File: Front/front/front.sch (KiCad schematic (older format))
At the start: 12 parts, among them J1 JST PH 1mm 4-Pin Connector, J2 Conn_01x10_Male, SW1 SW_Push, U1 L293D

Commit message: Version 0.1.2 - First draft of front PCB complete
Signed-off-by: ray33ee <30669752+ray33ee@users.noreply.github.com>
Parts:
- added C2: 100nF, Capacitor_SMD:C_1206_3216Metric_Pad1.33x1.80mm_HandSolder, symbol Device:C
- J1: value JST PH 1mm 4-Pin Connector -> JST 1mm Connector
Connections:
- net labels added: Enable_Controlled, Enable_High, JST_PIN_1, JST_PIN_2, JST_PIN_3, JST_PIN_4, Motor_Supply_Pre
- wire segments 57 -> 60
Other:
- moved on the sheet: C1, D1, D2, R1, R2, R3, R4
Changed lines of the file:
@@
 P 6400 3850
 F 0 "J1" H 6372 3732 50  0000 R CNN
-F 1 "JST PH 1mm 4-Pin Connector" H 6372 3823 50  0000 R CNN
+F 1 "JST 1mm Connector" H 6372 3823 50  0000 R CNN
 F 2 "Connector_JST:JST_SH_SM04B-SRSS-TB_1x04-1MP_P1.00mm_Horizontal" H 6400 3850 50  0001 C CNN
 F 3 "~" H 6400 3850 50  0001 C CNN
@@
 	-1   0    0    1
 $EndComp
-Wire Wire Line
-	5650 3650 6200 3650
 $Comp
 L Device:R R1
 U 1 1 616B895B
-P 5250 2800
-F 0 "R1" H 5320 2846 50  0000 L CNN
-F 1 "1" H 5320 2755 50  0000 L CNN
-F 2 "Resistor_THT:R_Axial_DIN0204_L3.6mm_D1.6mm_P5.08mm_Horizontal" V 5180 2800 50  0001 C CNN
-F 3 "~" H 5250 2800 50  0001 C CNN
-	1    5250 2800
+P 5250 2200
+F 0 "R1" H 5320 2246 50  0000 L CNN
+F 1 "1" H 5320 2155 50  0000 L CNN
+F 2 "Resistor_THT:R_Axial_DIN0204_L3.6mm_D1.6mm_P5.08mm_Horizontal" V 5180 2200 50  0001 C CNN
+F 3 "~" H 5250 2200 50  0001 C CNN
+	1    5250 2200
 	1    0    0    -1
 $EndComp
@@
 L Device:R R3
 U 1 1 616B9582
-P 6300 2550
-F 0 "R3" V 6093 2550 50  0000 C CNN
-F 1 "270" V 6184 2550 50  0000 C CNN
-F 2 "Resistor_SMD:R_1206_3216Metric_Pad1.30x1.75mm_HandSolder" V 6230 2550 50  0001 C CNN
-F 3 "~" H 6300 2550 50  0001 C CNN
-	1    6300 2550
+P 6300 1950
+F 0 "R3" V 6093 1950 50  0000 C CNN
+F 1 "270" V 6184 1950 50  0000 C CNN
+F 2 "Resistor_SMD:R_1206_3216Metric_Pad1.30x1.75mm_HandSolder" V 6230 1950 50  0001 C CNN
+F 3 "~" H 6300 1950 50  0001 C CNN
+	1    6300 1950
 	0    1    1    0
 $EndComp
@@
 L Device:R R4
 U 1 1 616B98B9
-P 4200 3000
-F 0 "R4" H 4270 3046 50  0000 L CNN
-F 1 "10k" H 4270 2955 50  0000 L CNN
-F 2 "Resistor_SMD:R_1206_3216Metric_Pad1.30x1.75mm_HandSolder" V 4130 3000 50  0001 C CNN
-F 3 "~" H 4200 3000 50  0001 C CNN
-	1    4200 3000
-	1    0    0    -1
-$EndComp
-Wire Wire Line
-	5250 2950 5250 3050
+P 3800 2400
+F 0 "R4" H 3870 2446 50  0000 L CNN
+F 1 "10k" H 3870 2355 50  0000 L CNN
+F 2 "Resistor_SMD:R_1206_3216Metric_Pad1.30x1.75mm_HandSolder" V 3730 2400 50  0001 C CNN
+F 3 "~" H 3800 2400 50  0001 C CNN
+	1    3800 2400
+	1    0    0    -1
+$EndComp
+Wire Wire Line
+	5250 2350 5250 2450
 $Comp
 L Device:D_Zener D2
 U 1 1 616BE794
-P 5700 2550
-F 0 "D2" H 5700 2767 50  0000 C CNN
-F 1 "3.9v" H 5700 2676 50  0000 C CNN
-F 2 "Diode_SMD:D_T-1_P5.08mm_Horizontal_SurfaceMount" H 5700 2550 50  0001 C CNN
-F 3 "~" H 5700 2550 50  0001 C CNN
-	1    5700 2550
+P 5700 1950
+F 0 "D2" H 5700 2167 50  0000 C CNN
+F 1 "3.9v" H 5700 2076 50  0000 C CNN
+F 2 "Diode_SMD:D_T-1_P5.08mm_Horizontal_SurfaceMount" H 5700 1950 50  0001 C CNN
+F 3 "~" H 5700 1950 50  0001 C CNN
+	1    5700 1950
 	1    0    0    -1
 $EndComp
@@
 L Device:D_Zener D1
 U 1 1 616C048F
-P 5700 3050
-F 0 "D1" H 5700 3267 50  0000 C CNN
-F 1 "3.9v" H 5700 3176 50  0000 C CNN
-F 2 "Diode_SMD:D_T-1_P5.08mm_Horizontal_SurfaceMount" H 5700 3050 50  0001 C CNN
-F 3 "~" H 5700 3050 50  0001 C CNN
-	1    5700 3050
-	1    0    0    -1
-$EndComp
-Wire Wire Line
-	5550 2550 5250 2550
-Connection ~ 5250 2550
-Wire Wire Line
-	5250 2550 5250 2650
-Wire Wire Line
-	5250 3050 5550 3050
-Connection ~ 5250 3050
-Wire Wire Line
-	5250 3050 5250 3250
-Wire Wire Line
-	5850 2550 6000 2550
-Wire Wire Line
-	6150 3050 6000 3050
-Wire Wire Line
-	6450 3050 6450 2550
-Wire Wire Line
-	5050 3250 5050 2800
-Connection ~ 5050 2550
-Wire Wire Line
-	5050 2550 5250 2550
+P 5700 2450
+F 0 "D1" H 5700 2667 50  0000 C CNN
+F 1 "3.9v" H 5700 2576 50  0000 C CNN
+F 2 "Diode_SMD:D_T-1_P5.08mm_Horizontal_SurfaceMount" H 5700 2450 50  0001 C CNN
+F 3 "~" H 5700 2450 50  0001 C CNN
+	1    5700 2450
+	1    0    0    -1
+$EndComp
+Wire Wire Line
+	5550 1950 5250 1950
+Connection ~ 5250 1950
+Wire Wire Line
+	5250 1950 5250 2050
+Wire Wire Line
+	5250 2450 5550 2450
+Connection ~ 5250 2450
+Wire Wire Line
+	5850 1950 6000 1950
+Wire Wire Line
+	6150 2450 6000 2450
+Wire Wire Line
+	6450 2450 6450 1950
+Connection ~ 5050 1950
+Wire Wire Line
+	5050 1950 5250 1950
 $Comp
 L Device:R R2
 U 1 1 616B8410
-P 6300 3050
-F 0 "R2" V 6507 3050 50  0000 C CNN
-F 1 "270" V 6416 3050 50  0000 C CNN
-F 2 "Resistor_SMD:R_1206_3216Metric_Pad1.30x1.75mm_HandSolder" V 6230 3050 50  0001 C CNN
-F 3 "~" H 6300 3050 50  0001 C CNN
-	1    6300 3050
+P 6300 2450
+F 0 "R2" V 6507 2450 50  0000 C CNN
+F 1 "270" V 6416 2450 50  0000 C CNN
+F 2 "Resistor_SMD:R_1206_3216Metric_Pad1.30x1.75mm_HandSolder" V 6230 2450 50  0001 C CNN
+F 3 "~" H 6300 2450 50  0001 C CNN
+	1    6300 2450
 	0    -1   -1   0
 $EndComp
@@
 L power:GND #PWR0103
 U 1 1 616C51FA
-P 6800 3100
-F 0 "#PWR0103" H 6800 2850 50  0001 C CNN
-F 1 "GND" H 6805 2927 50  0000 C CNN
-F 2 "" H 6800 3100 50  0001 C CNN
-F 3 "" H 6800 3100 50  0001 C CNN
-	1    6800 3100
-	1    0    0    -1
-$EndComp
-Wire Wire Line
-	6800 3050 6800 3100
-Wire Wire Line
-	6000 2550 6000 2750
-Wire Wire Line
-	6000 2750 6350 2750
-Connection ~ 6000 2550
-Wire Wire Line
-	6000 2550 6150 2550
-Wire Wire Line
-	6000 3050 6000 3250
-Wire Wire Line
-	6000 3250 6350 3250
-Wire Wire Line
-	6450 3050 6800 3050
-Connection ~ 6450 3050
-Connection ~ 6000 3050
-Wire Wire Line
-	6000 3050 5850 3050
-Wire Wire Line
-	4200 2850 4200 2550
+P 6800 2500
+F 0 "#PWR0103" H 6800 2250 50  0001 C CNN
+F 1 "GND" H 6805 2327 50  0000 C CNN
+F 2 "" H 6800 2500 50  0001 C CNN
+F 3 "" H 6800 2500 50  0001 C CNN
+	1    6800 2500
+	1    0    0    -1
+$EndComp
+Wire Wire Line
+	6800 2450 6800 2500
+Wire Wire Line
+	6000 1950 6000 2150
+Wire Wire Line
+	6000 2150 6350 2150
+Connection ~ 6000 1950
+Wire Wire Line
+	6000 1950 6150 1950
+Wire Wire Line
+	6000 2450 6000 2650
+Wire Wire Line
+	6000 2650 6350 2650
+Wire Wire Line
+	6450 2450 6800 2450
+Connection ~ 6450 2450
+Connection ~ 6000 2450
+Wire Wire Line
+	6000 2450 5850 2450
+Wire Wire Line
+	3800 2250 3800 1950
 Wire Wire Line
 	4650 3650 4300 3650
@@
 	6500 4850 7050 4850
 Wire Wire Line
-	4200 2550 5050 2550
+	4200 1950 5050 1950
 $Comp
 L Connector:Conn_01x10_Male J2
@@
 Text Label 4350 4450 0    50   ~ 0
 Coil_B2
-Text Label 3350 3000 0    50   ~ 0
-Enable
-Text Label 6050 2750 0    50   ~ 0
+Text Label 4200 3250 1    50   ~ 0
+Enable_Controlled
+Text Label 6050 2150 0    50   ~ 0
 Diff_P1
-Text Label 6050 3250 0    50   ~ 0
+Text Label 6050 2650 0    50   ~ 0
 Diff_P2
 Text Label 8050 4100 0    50   ~ 0
@@
 	8000 4200 8550 4200
 Text Label 8050 4000 0    50   ~ 0
-Enable
+Enable_Controlled
 Text Label 8050 3800 0    50   ~ 0
 Diff_P2
@@
 	4000 4050 4000 4650
 Wire Wire Line
-	4200 3150 4200 3500
-Wire Wire Line
-	3800 3500 3800 3000
-Wire Wire Line
-	3200 3000 3800 3000
-Wire Wire Line
 	4950 5050 5050 5050
 Connection ~ 5050 5050
@@
 $EndComp
 Wire Wire Line
-	5650 3850 6200 3850
-Wire Wire Line
 	5650 4250 5700 4250
 Wire Wire Line
@@
 L Device:C C1
 U 1 1 61713F7C
-P 4550 2950
-F 0 "C1" H 4665 2996 50  0000 L CNN
-F 1 "100nF" H 4665 2905 50  0000 L CNN
-F 2 "Capacitor_SMD:C_1206_3216Metric_Pad1.33x1.80mm_HandSolder" H 4588 2800 50  0001 C CNN
-F 3 "~" H 4550 2950 50  0001 C CNN
-	1    4550 2950
-	1    0    0    -1
-$EndComp
-Connection ~ 5050 2800
-Wire Wire Line
-	5050 2800 5050 2550
+P 4650 2850
+F 0 "C1" H 4765 2896 50  0000 L CNN
+F 1 "100nF" H 4765 2805 50  0000 L CNN
+F 2 "Capacitor_SMD:C_1206_3216Metric_Pad1.33x1.80mm_HandSolder" H 4688 2700 50  0001 C CNN
+F 3 "~" H 4650 2850 50  0001 C CNN
+	1    4650 2850
+	1    0    0    -1
+$EndComp
+Connection ~ 5050 2200
+Wire Wire Line
+	5050 2200 5050 1950
 $Comp
 L power:GND #PWR0107
 U 1 1 61715C98
-P 4550 3100
-F 0 "#PWR0107" H 4550 2850 50  0001 C CNN
-F 1 "GND" H 4555 2927 50  0000 C CNN
-F 2 "" H 4550 3100 50  0001 C CNN
-F 3 "" H 4550 3100 50  0001 C CNN
-	1    4550 3100
-	1    0    0    -1
-$EndComp
-Wire Wire Line
-	4550 2800 5050 2800
+P 4650 3000
+F 0 "#PWR0107" H 4650 2750 50  0001 C CNN
+F 1 "GND" H 4655 2827 50  0000 C CNN
+F 2 "" H 4650 3000 50  0001 C CNN
+F 3 "" H 4650 3000 50  0001 C CNN
+	1    4650 3000
+	1    0    0    -1
+$EndComp
 $Comp
 L power:+5V #PWR0102
 U 1 1 616B66D4
-P 4200 2550
-F 0 "#PWR0102" H 4200 2400 50  0001 C CNN
-F 1 "+5V" H 4215 2723 50  0000 C CNN
-F 2 "" H 4200 2550 50  0001 C CNN
-F 3 "" H 4200 2550 50  0001 C CNN
-	1    4200 2550
-	1    0    0    -1
-$EndComp
-Connection ~ 4200 2550
+P 4200 1950
+F 0 "#PWR0102" H 4200 1800 50  0001 C CNN
+F 1 "+5V" H 4215 2123 50  0000 C CNN
+F 2 "" H 4200 1950 50  0001 C CNN
+F 3 "" H 4200 1950 50  0001 C CNN
+	1    4200 1950
+	1    0    0    -1
+$EndComp
+Text Label 5250 2600 0    50   ~ 0
+Motor_Supply_Pre
+Text Label 5750 3750 0    50   ~ 0
+JST_PIN_3
+Text Label 5750 3950 0    50   ~ 0
+JST_PIN_1
+Text Label 4350 4050 0    50   ~ 0
+Enable
+Text Label 3800 2850 2    50   ~ 0
+Enable_High
+Wire Wire Line
+	5250 2450 5250 2700
+$Comp
+L Device:C C2
+U 1 1 616EC3C1
+P 5600 2850
+F 0 "C2" H 5715 2896 50  0000 L CNN
+F 1 "100nF" H 5715 2805 50  0000 L CNN
+F 2 "Capacitor_SMD:C_1206_3216Metric_Pad1.33x1.80mm_HandSolder" H 5638 2700 50  0001 C CNN
+F 3 "~" H 5600 2850 50  0001 C CNN
+	1    5600 2850
+	1    0    0    -1
+$EndComp
+$Comp
+L power:GND #PWR0108
+U 1 1 616EC3C7
+P 5600 3000
+F 0 "#PWR0108" H 5600 2750 50  0001 C CNN
+F 1 "GND" H 5605 2827 50  0000 C CNN
+F 2 "" H 5600 3000 50  0001 C CNN
+F 3 "" H 5600 3000 50  0001 C CNN
+	1    5600 3000
+	1    0    0    -1
+$EndComp
+Wire Wire Line
+	3800 2550 3800 3500
+Wire Wire Line
+	4650 2700 4650 2200
+Wire Wire Line
+	4650 2200 5050 2200
+Wire Wire Line
+	5600 2700 5250 2700
+Connection ~ 5250 2700
+Wire Wire Line
+	5250 2700 5250 3250
+Wire Wire Line
+	5050 2200 5050 3250
+Wire Wire Line
+	3800 1950 4200 1950
+Connection ~ 4200 1950
+Wire Wire Line
+	4200 3500 4200 2550
+Text Label 5750 3850 0    50   ~ 0
+JST_PIN_2
+Wire Wire Line
+	5650 3850 6200 3850
+Text Label 5750 3650 0    50   ~ 0
+JST_PIN_4
+Wire Wire Line
+	5650 3650 6200 3650
 $EndSCHEMATC

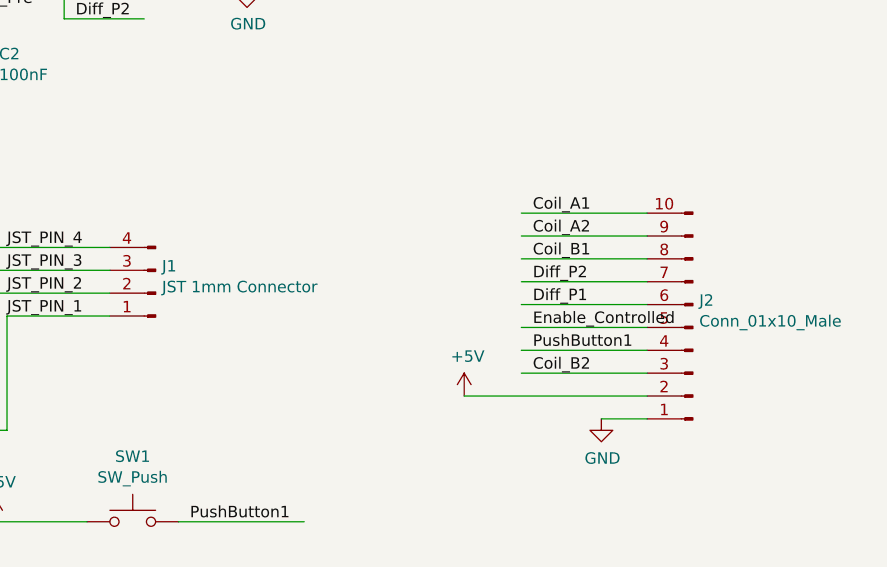
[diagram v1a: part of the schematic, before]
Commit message: Version 0.1.3 - Various changes, see changelog
Signed-off-by: ray33ee <30669752+ray33ee@users.noreply.github.com>
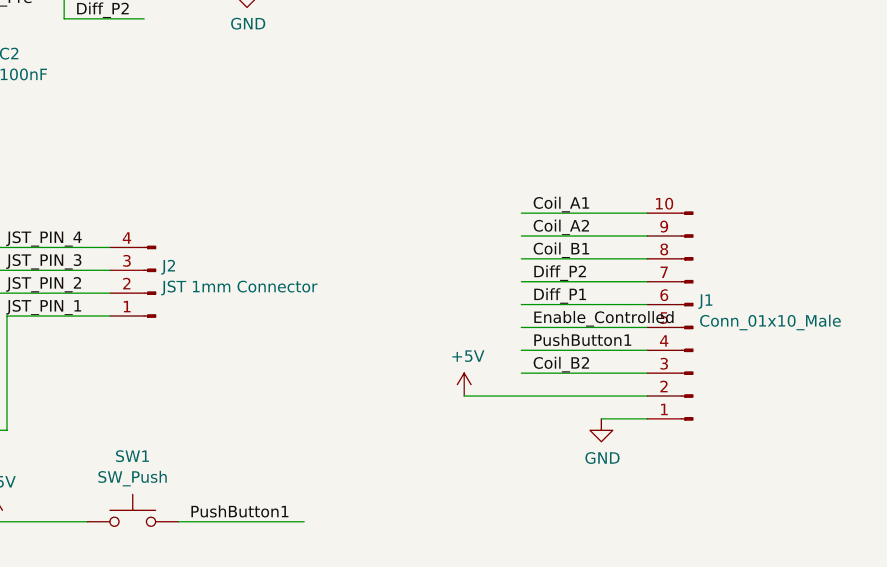
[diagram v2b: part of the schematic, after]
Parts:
- renumbered J2 to J1, J1 to J2
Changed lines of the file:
@@
 	5350 5050 5350 5150
 $Comp
-L Connector:Conn_01x04_Male J1
+L Connector:Conn_01x04_Male J2
 U 1 1 616B3A80
 P 6400 3850
-F 0 "J1" H 6372 3732 50  0000 R CNN
+F 0 "J2" H 6372 3732 50  0000 R CNN
 F 1 "JST 1mm Connector" H 6372 3823 50  0000 R CNN
 F 2 "Connector_JST:JST_SH_SM04B-SRSS-TB_1x04-1MP_P1.00mm_Horizontal" H 6400 3850 50  0001 C CNN
@@
 	4200 1950 5050 1950
 $Comp
-L Connector:Conn_01x10_Male J2
+L Connector:Conn_01x10_Male J1
 U 1 1 616DA38A
 P 8750 4000
-F 0 "J2" H 8722 3882 50  0000 R CNN
+F 0 "J1" H 8722 3882 50  0000 R CNN
 F 1 "Conn_01x10_Male" H 8722 3973 50  0000 R CNN
 F 2 "Connector_PinHeader_2.54mm:PinHeader_1x10_P2.54mm_Vertical" H 8750 4000 50  0001 C CNN

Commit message: Version 0.1.7 - Various changes, see changelog
Signed-off-by: ray33ee <30669752+ray33ee@users.noreply.github.com>
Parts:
- removed JP1: SolderJumper_3_Open, Jumper:SolderJumper-3_P1.3mm_Open_RoundedPad1.0x1.5mm_NumberLabels, symbol Jumper:SolderJumper_3_Open
- added JP1: SolderJumper_3_Bridged12, Jumper:SolderJumper-3_P1.3mm_Bridged12_RoundedPad1.0x1.5mm_NumberLabels, symbol Jumper:SolderJumper_3_Bridged12
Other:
- moved on the sheet: R4
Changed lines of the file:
@@
 L Device:R R4
 U 1 1 616B98B9
-P 3800 2400
-F 0 "R4" H 3870 2446 50  0000 L CNN
-F 1 "10k" H 3870 2355 50  0000 L CNN
-F 2 "Resistor_SMD:R_1206_3216Metric_Pad1.30x1.75mm_HandSolder" V 3730 2400 50  0001 C CNN
-F 3 "~" H 3800 2400 50  0001 C CNN
-	1    3800 2400
+P 4200 2400
+F 0 "R4" H 4270 2446 50  0000 L CNN
+F 1 "10k" H 4270 2355 50  0000 L CNN
+F 2 "Resistor_SMD:R_1206_3216Metric_Pad1.30x1.75mm_HandSolder" V 4130 2400 50  0001 C CNN
+F 3 "~" H 4200 2400 50  0001 C CNN
+	1    4200 2400
 	1    0    0    -1
 $EndComp
@@
 	6150 2450 6000 2450
 Wire Wire Line
-	6450 2450 6450 1950
+	6800 2450 6800 1950
 Connection ~ 5050 1950
 Wire Wire Line
@@
 Wire Wire Line
 	6450 2450 6800 2450
-Connection ~ 6450 2450
 Connection ~ 6000 2450
 Wire Wire Line
 	6000 2450 5850 2450
 Wire Wire Line
-	3800 2250 3800 1950
+	4200 2250 4200 1950
 Wire Wire Line
 	4650 3650 4300 3650
@@
 	-1   0    0    1
 $EndComp
-Text Label 6550 4850 0    50   ~ 0
+Text Label 7050 4850 2    50   ~ 0
 PushButton1
 Text Label 4350 3650 0    50   ~ 0
@@
 Text Label 4350 4450 0    50   ~ 0
 Coil_B2
-Text Label 4200 3250 1    50   ~ 0
+Text Label 3800 2550 3    50   ~ 0
 Enable_Controlled
-Text Label 6050 2150 0    50   ~ 0
+Text Label 6350 2150 2    50   ~ 0
 Diff_P1
-Text Label 6050 2650 0    50   ~ 0
+Text Label 6350 2650 2    50   ~ 0
 Diff_P2
-Text Label 8050 4100 0    50   ~ 0
+Text Label 8000 4100 0    50   ~ 0
 PushButton1
 Wire Wire Line
@@
 Wire Wire Line
 	8000 4200 8550 4200
-Text Label 8050 4000 0    50   ~ 0
+Text Label 8000 4000 0    50   ~ 0
 Enable_Controlled
-Text Label 8050 3800 0    50   ~ 0
+Text Label 8000 3800 0    50   ~ 0
 Diff_P2
-Text Label 8050 3900 0    50   ~ 0
+Text Label 8000 3900 0    50   ~ 0
 Diff_P1
-Text Label 8050 3500 0    50   ~ 0
+Text Label 8000 3500 0    50   ~ 0
 Coil_A1
-Text Label 8050 3600 0    50   ~ 0
+Text Label 8000 3600 0    50   ~ 0
 Coil_A2
-Text Label 8050 3700 0    50   ~ 0
+Text Label 8000 3700 0    50   ~ 0
 Coil_B1
-Text Label 8050 4200 0    50   ~ 0
+Text Label 8000 4200 0    50   ~ 0
 Coil_B2
 $Comp
@@
 Wire Wire Line
 	8350 4400 8550 4400
-$Comp
-L Jumper:SolderJumper_3_Open JP1
-U 1 1 616F3485
-P 4000 3500
-F 0 "JP1" H 4000 3705 50  0000 C CNN
-F 1 "SolderJumper_3_Open" H 4050 3600 50  0000 C CNN
-F 2 "Jumper:SolderJumper-3_P1.3mm_Open_RoundedPad1.0x1.5mm_NumberLabels" H 4000 3500 50  0001 C CNN
-F 3 "~" H 4000 3500 50  0001 C CNN
-	1    4000 3500
-	1    0    0    -1
-$EndComp
 Wire Wire Line
 	4000 3650 4000 4050
@@
 Text Label 4350 4050 0    50   ~ 0
 Enable
-Text Label 3800 2850 2    50   ~ 0
+Text Label 4200 2550 3    50   ~ 0
 Enable_High
 Wire Wire Line
@@
 $EndComp
 Wire Wire Line
-	3800 2550 3800 3500
+	4200 2550 4200 3500
 Wire Wire Line
 	4650 2700 4650 2200
@@
 Wire Wire Line
 	5050 2200 5050 3250
-Wire Wire Line
-	3800 1950 4200 1950
 Connection ~ 4200 1950
 Wire Wire Line
-	4200 3500 4200 2550
+	3800 3500 3800 2550
 Text Label 5750 3850 0    50   ~ 0
 JST_PIN_2
@@
 Wire Wire Line
 	5650 3650 6200 3650
+$Comp
+L Jumper:SolderJumper_3_Bridged12 JP1
+U 1 1 61707BB6
+P 4000 3500
+F 0 "JP1" H 4000 3705 50  0000 C CNN
+F 1 "SolderJumper_3_Bridged12" H 4000 3614 50  0000 C CNN
+F 2 "Jumper:SolderJumper-3_P1.3mm_Bridged12_RoundedPad1.0x1.5mm_NumberLabels" H 4000 3500 50  0001 C CNN
+F 3 "~" H 4000 3500 50  0001 C CNN
+	1    4000 3500
+	1    0    0    -1
+$EndComp
+Connection ~ 6800 2450
+Wire Wire Line
+	6450 1950 6800 1950
 $EndSCHEMATC

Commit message: Version 0.1.15 - Various changes, see changelog
Signed-off-by: ray33ee <30669752+ray33ee@users.noreply.github.com>
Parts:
- R1: footprint Resistor_THT:R_Axial_DIN0204_L3.6mm_D1.6mm_P5.08mm_Horizontal -> Resistor_THT:R_Axial_DIN0204_L3.6mm_D1.6mm_P7.62mm_Horizontal
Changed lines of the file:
@@
 F 0 "R1" H 5320 2246 50  0000 L CNN
 F 1 "1" H 5320 2155 50  0000 L CNN
-F 2 "Resistor_THT:R_Axial_DIN0204_L3.6mm_D1.6mm_P5.08mm_Horizontal" V 5180 2200 50  0001 C CNN
+F 2 "Resistor_THT:R_Axial_DIN0204_L3.6mm_D1.6mm_P7.62mm_Horizontal" V 5180 2200 50  0001 C CNN
 F 3 "~" H 5250 2200 50  0001 C CNN
 	1    5250 2200

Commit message: Version 0.1.16 - Various changes, see changelog
Signed-off-by: ray33ee <30669752+ray33ee@users.noreply.github.com>
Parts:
- D1, D2: footprint Diode_SMD:D_T-1_P5.08mm_Horizontal_SurfaceMount -> Diode_SMD:D_MiniMELF
- R1: footprint Resistor_THT:R_Axial_DIN0204_L3.6mm_D1.6mm_P7.62mm_Horizontal -> Resistor_SMD:R_1206_3216Metric_Pad1.30x1.75mm_HandSolder
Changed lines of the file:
@@
 F 0 "R1" H 5320 2246 50  0000 L CNN
 F 1 "1" H 5320 2155 50  0000 L CNN
-F 2 "Resistor_THT:R_Axial_DIN0204_L3.6mm_D1.6mm_P7.62mm_Horizontal" V 5180 2200 50  0001 C CNN
+F 2 "Resistor_SMD:R_1206_3216Metric_Pad1.30x1.75mm_HandSolder" V 5180 2200 50  0001 C CNN
 F 3 "~" H 5250 2200 50  0001 C CNN
 	1    5250 2200
@@
 F 0 "D2" H 5700 2167 50  0000 C CNN
 F 1 "3.9v" H 5700 2076 50  0000 C CNN
-F 2 "Diode_SMD:D_T-1_P5.08mm_Horizontal_SurfaceMount" H 5700 1950 50  0001 C CNN
+F 2 "Diode_SMD:D_MiniMELF" H 5700 1950 50  0001 C CNN
 F 3 "~" H 5700 1950 50  0001 C CNN
 	1    5700 1950
@@
 F 0 "D1" H 5700 2667 50  0000 C CNN
 F 1 "3.9v" H 5700 2576 50  0000 C CNN
-F 2 "Diode_SMD:D_T-1_P5.08mm_Horizontal_SurfaceMount" H 5700 2450 50  0001 C CNN
+F 2 "Diode_SMD:D_MiniMELF" H 5700 2450 50  0001 C CNN
 F 3 "~" H 5700 2450 50  0001 C CNN
 	1    5700 2450
